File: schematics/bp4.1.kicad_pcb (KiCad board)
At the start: 2 copper layers, 90 x 32.6 mm, 39 parts, among them J1 Left Pin Strip, J2 Right Pin Strip, J3 I/O Pin Strip, J4 Power Pins A, J5 Power Pins B, J6 Power Pins C, SW1 Power Switch, U1 TPS61220DCK, U2 LM321

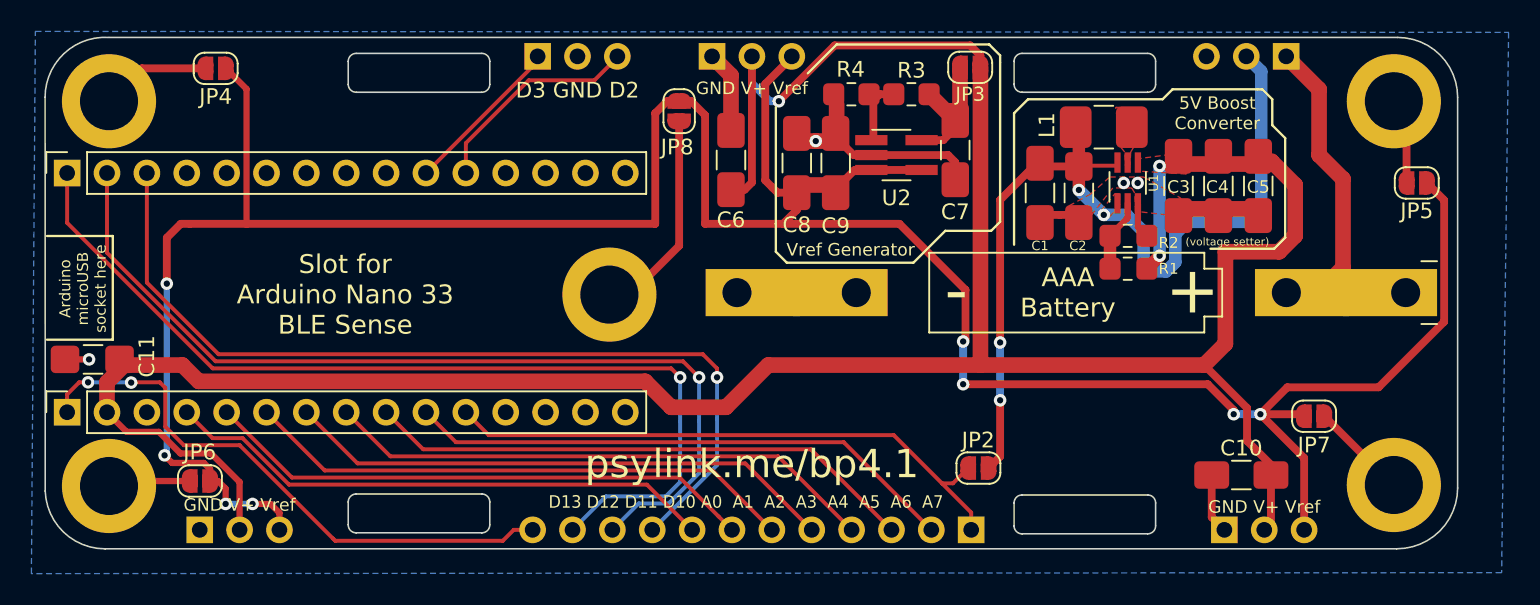
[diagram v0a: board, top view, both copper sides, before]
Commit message: update bp4.1 to include external power supply + power LED
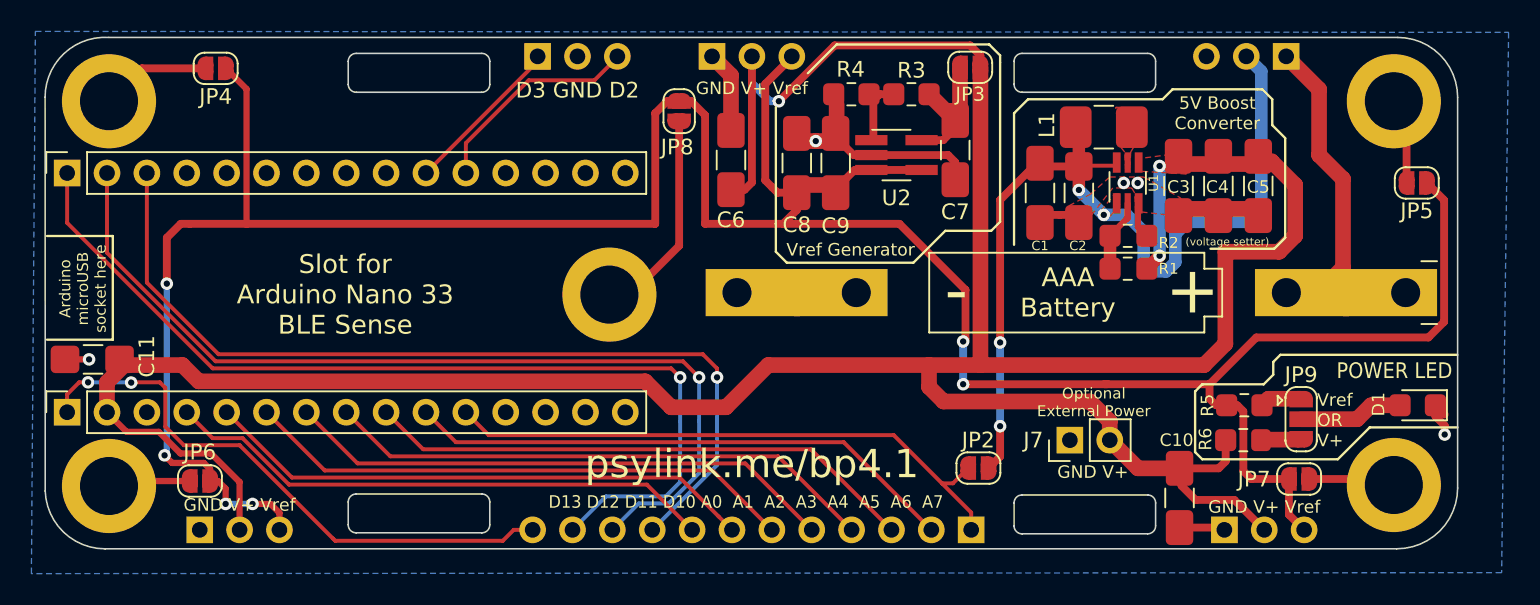
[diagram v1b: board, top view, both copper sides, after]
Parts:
- added D1: Power LED, LED_SMD:LED_0805_2012Metric_Pad1.15x1.40mm_HandSolder, F.Cu at (112.8, 48.8)
- added J7: External Power, Connector_PinHeader_2.54mm:PinHeader_1x02_P2.54mm_Vertical, F.Cu at (90.7, 51.1)
- added JP9: Power LED Config Jumper, Jumper:SolderJumper-3_P1.3mm_Open_RoundedPad1.0x1.5mm, F.Cu at (105.4, 49.7)
- added R5: 22/5%, Resistor_SMD:R_0805_2012Metric_Pad1.15x1.40mm_HandSolder, F.Cu at (101.8, 48.8)
- added R6: 110/5%, Resistor_SMD:R_0805_2012Metric_Pad1.15x1.40mm_HandSolder, F.Cu at (101.7, 51.1)
- moved C10 4.20 mm to (97.7, 54.7), turned to 270 degrees
- moved JP7 4.11 mm to (105.3, 53.5)
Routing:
- net /V+: track 178.9 -> 199.3 mm
- net Net-(D1-Pad2): track 0.00 -> 6.67 mm
- net Net-(JP9-Pad1): track 0.00 -> 2.66 mm
- net Net-(JP9-Pad3): track 0.00 -> 2.62 mm
- net /GND: track 33.6 -> 36.0 mm, vias 4 -> 5
- net /Vref: track 184.8 -> 185.8 mm, vias 8 -> 6
- net Net-(JP7-Pad2): track 6.24 -> 5.59 mm
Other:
- board text added: "GND V+"
- board text added: "Optional External Power"
- board text added: "POWER LED"
- board text added: "Vref OR V+"
